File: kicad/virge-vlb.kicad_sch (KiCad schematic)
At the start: 41 parts, among them CN1 VGA, U1 86C325, Y1 14.318MHz

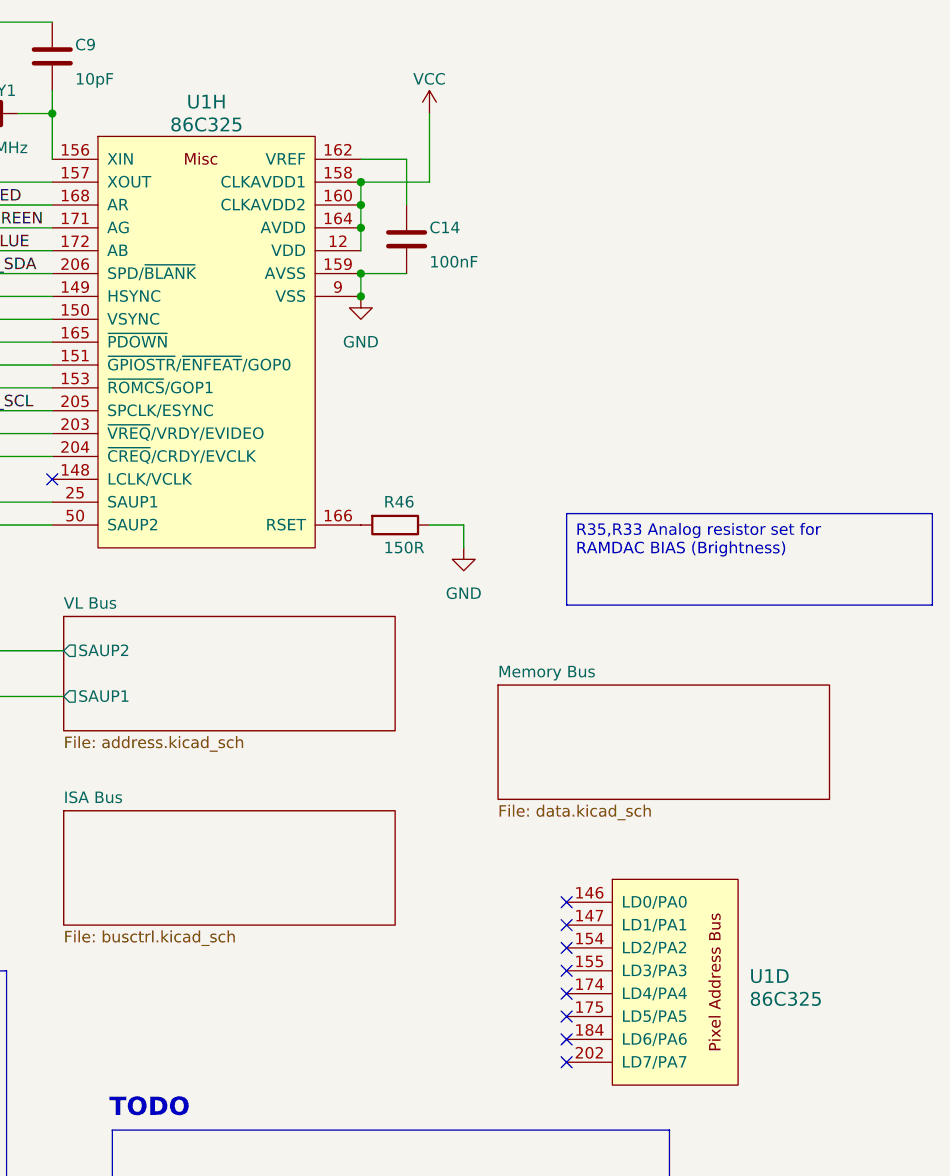
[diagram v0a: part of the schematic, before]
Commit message: updated VLB footprint
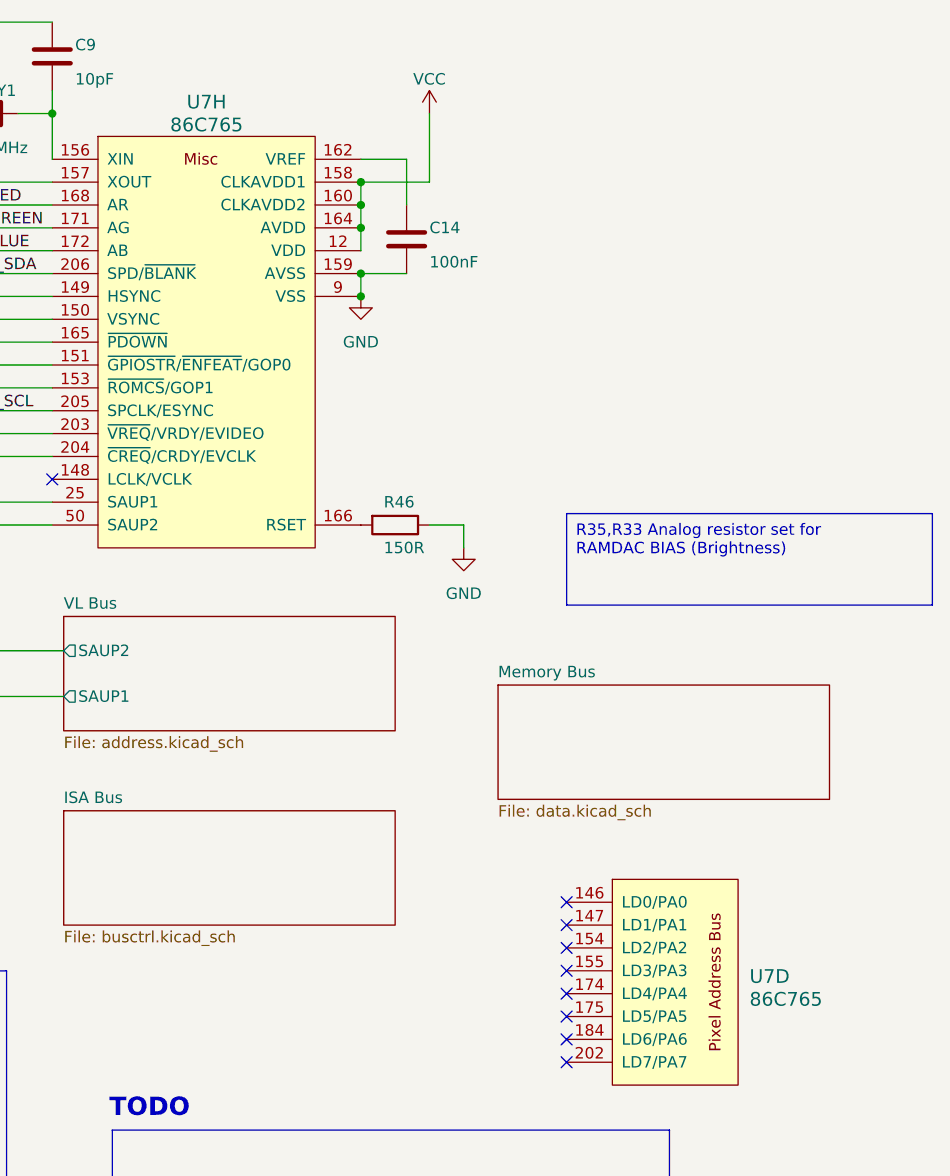
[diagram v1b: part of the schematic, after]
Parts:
- removed U1: 86C325, VLB:QFP-208, symbol virge:86C375
- added U7: 86C765, Package_QFP:PQFP-208_28x28mm_P0.5mm, symbol virge:86C765
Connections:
- net DDC_SCL: now also U7.205 (SPCLK/ESYNC)
- net DDC_SDA: now also U7.206 (SPD/~{BLANK})
- net GND: now also U7.114 (VSS), U7.123 (VSS), U7.126 (VSS), U7.135 (VSS), U7.145 (VSS), U7.159 (AVSS), U7.161 (AVSS), U7.163 (AVSS), U7.167 (AVSS), U7.173 (AVSS), U7.195 (VSS), U7.22 (VSS), U7.32 (VSS), U7.47 (VSS), U7.60 (VSS), U7.71 (VSS), U7.87 (VSS), U7.9 (VSS), U7.99 (VSS)
- net HS: now also U7.149 (HSYNC)
- net ROMCS: now also U7.153 (~{ROMCS}/GOP1)
- net S3_BLUE: now also U7.172 (AB)
- net S3_GREEN: now also U7.171 (AG)
- net S3_RED: now also U7.168 (AR)
- net VCC: now also U7.12 (VDD), U7.137 (VDD), U7.158 (CLKAVDD1), U7.160 (CLKAVDD2), U7.164 (AVDD), U7.169 (AVDD), U7.170 (AVDD), U7.192 (VDD), U7.37 (VDD), U7.62 (VDD), U7.81 (VDD), U7.96 (VDD)
- net VL Bus/SAUP1: now also U7.25 (SAUP1)
- net VL Bus/SAUP2: now also U7.50 (SAUP2)
- net VS: now also U7.150 (VSYNC)
- net at C9.2, Y1.2: now also U7.156 (XIN)
- net at R42.1: now also U7.204 (~{CREQ}/CRDY/EVCLK)
- net at C10.2, Y1.1: now also U7.157 (XOUT)
- net at C14.1: now also U7.162 (VREF)
- net at R22.1: now also U7.165 (~{PDOWN})
- net at R46.2: now also U7.166 (RSET)
- net at R43.1: now also U7.203 (~{VREQ}/VRDY/EVIDEO)

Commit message: fixed VGA footprint
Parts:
- U7: footprint Package_QFP:PQFP-208_28x28mm_P0.5mm -> VLB:QFP-208
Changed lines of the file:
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@@
       (effects (font (size 1.524 1.524)))
     )
-    (property "Footprint" "Package_QFP:PQFP-208_28x28mm_P0.5mm" (at 149.86 49.53 0)
+    (property "Footprint" "VLB:QFP-208" (at 149.86 49.53 0)
       (effects (font (size 1.524 1.524)) (justify right) hide)
     )
@@
       (effects (font (size 1.524 1.524)) (justify left))
     )
-    (property "Footprint" "Package_QFP:PQFP-208_28x28mm_P0.5mm" (at 201.93 123.19 0)
+    (property "Footprint" "VLB:QFP-208" (at 201.93 123.19 0)
       (effects (font (size 1.524 1.524)) (justify right) hide)
     )

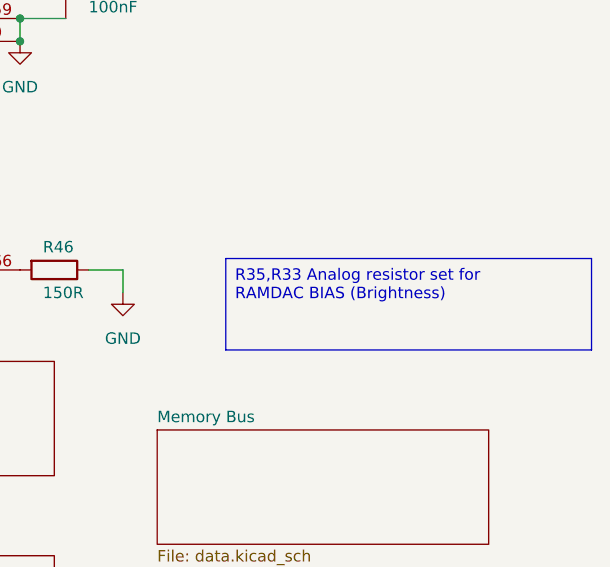
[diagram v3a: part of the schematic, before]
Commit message: updated to kicad 9
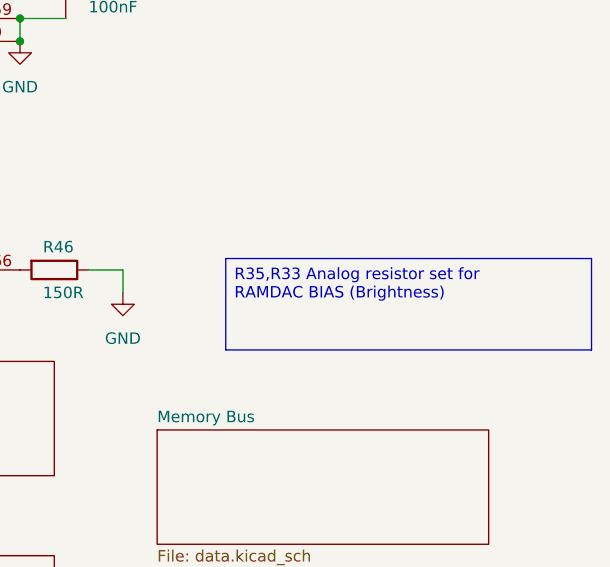
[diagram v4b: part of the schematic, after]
